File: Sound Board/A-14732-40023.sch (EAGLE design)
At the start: 237 parts, among them P2 AUX IN, P3 AUX OUT, P4 ORKIN R/W, P5 VOLUME, P6 0.156", P7 0.156", Q1 MPS3646, U1 OKI6295, U10 26LS32A, U11 26LS31, U12 27C040-150, U13 27C040-150, U14 YAMAHA 2151, U15 TIL7524, U16 74LS374, U17 74LS174, U18 16L8, U19 74LS11, U2 2064, U20 74LS139, U21 74LS14, U22 74LS74, U23 74LS74, U24 26LS31, U25 26LS32A, U26 74LS04, U28 YAMAHA 3012, U29 LM324D, U3 27C040, U30 MC3340, U31 MB3731, U32 TL084D, U33 TL084D, U4 6809E, U5 74LS374DW, U6 26LS32A, U7 26LS31, U8 74LS138, U9 74LS74, Y1 3.5749MHz, Y2 8MHz

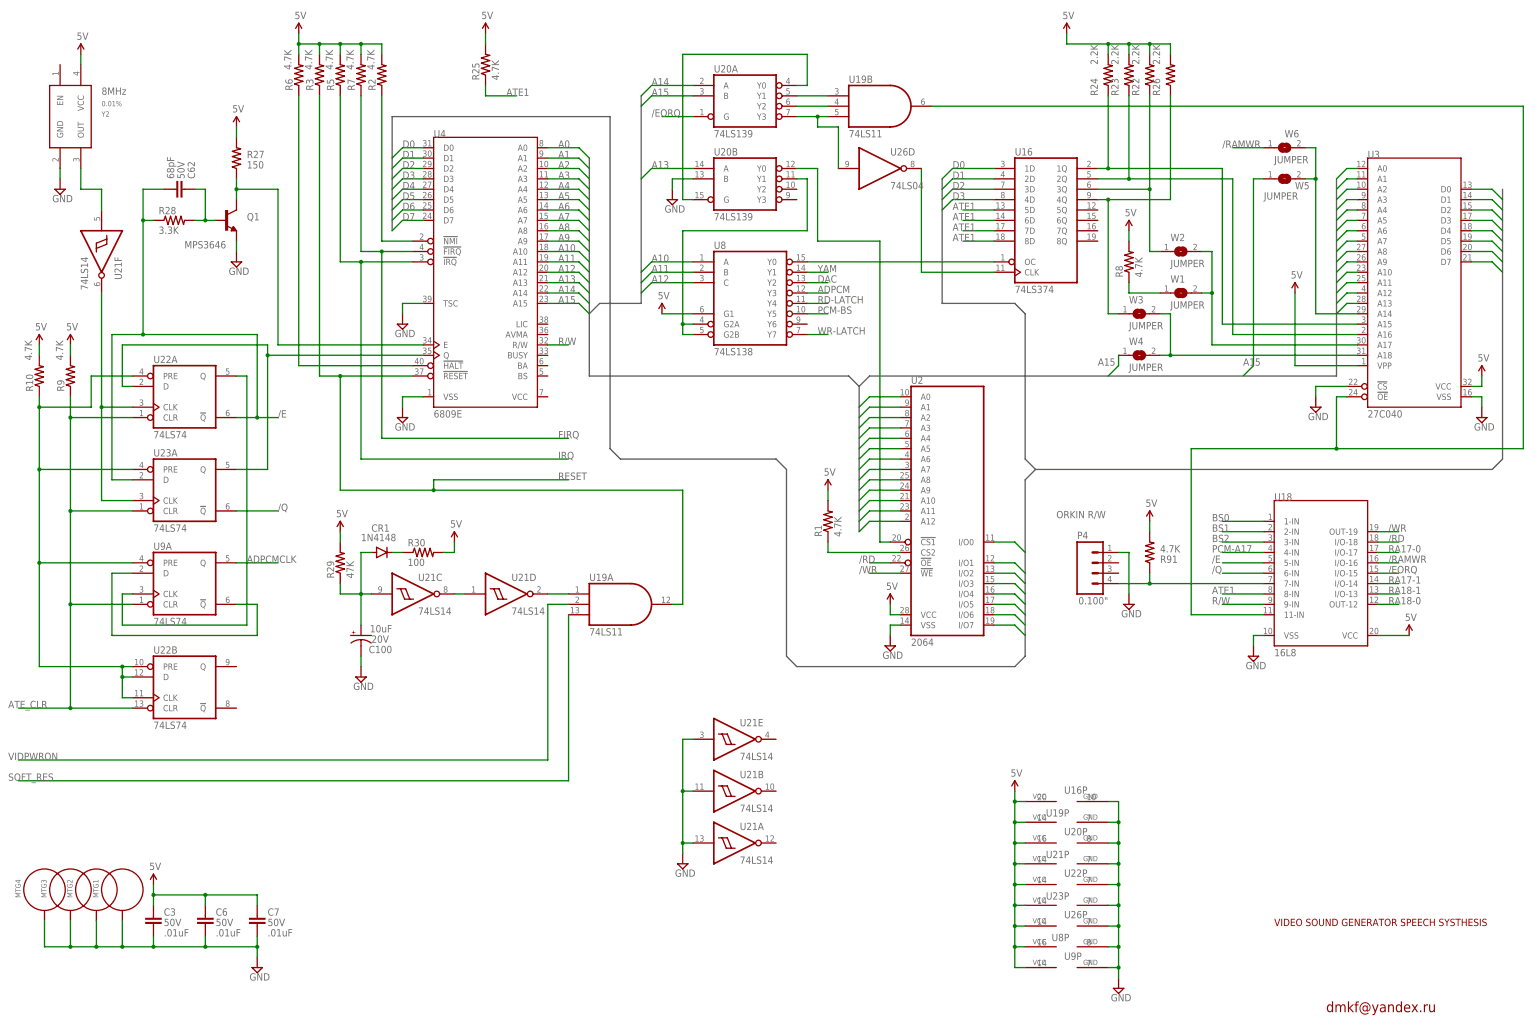
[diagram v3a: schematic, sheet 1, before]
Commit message: replaced all non-power rail resistors to 0805 size 1/8W
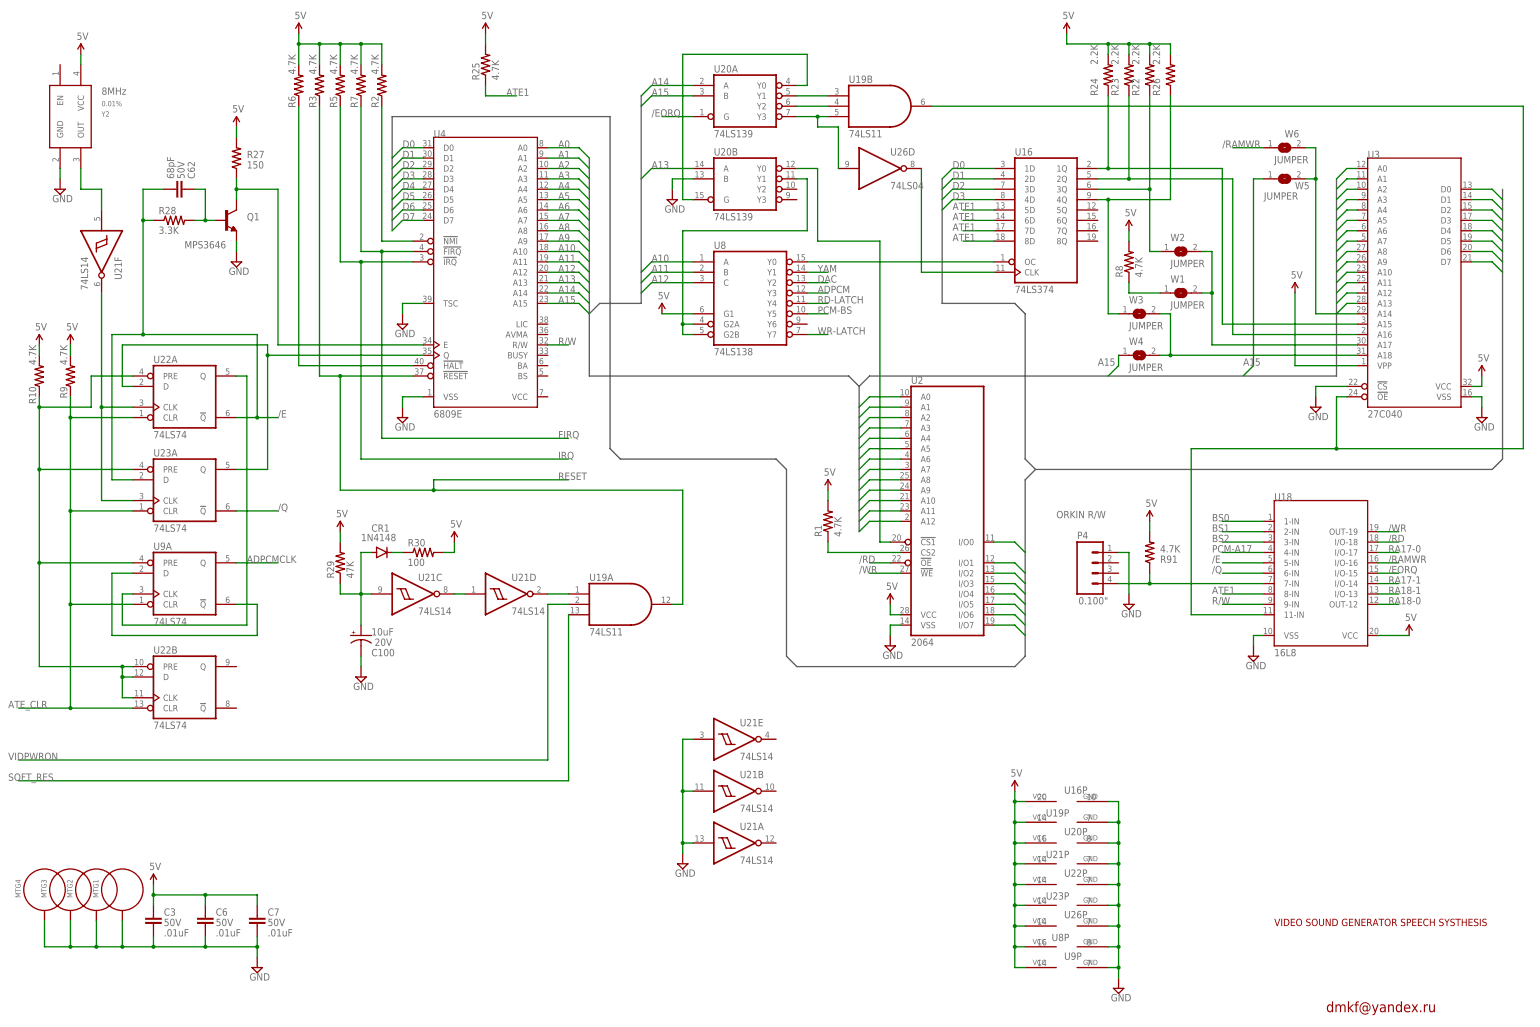
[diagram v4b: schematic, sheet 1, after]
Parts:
- C100: device SparkFun-Capacitors:10UF-16V-10%(TANT) -> A-14732-40023:CAP_POLC
- C3, C6, C61, C62, C7: device SparkFun-Capacitors:1.0UF50V10%(1206) -> SparkFun-Passives:CAP0805
- R10, R11, R12, R13, R14, R19, R2, R20, R21, R22, R23, R24, R25, R26, R28, R29, R3, R32, R33, R34, R35, R36, R37, R38, R39, R4, R40, R41, R42, R43, R44, R45, R46, R48, R5, R51, R52, R53, R55, R59, R6, R60, R61, R62, R63, R64, R67, R68, R69, R7, R71, R77, R78, R79, R80, R81, R84, R85, R86, R87, R88, R9, R91, R92, R93, R94, R95, R96: device resistor:R-US_R1206 -> SparkFun-Passives:RESISTOR0805-RES
- R27, R30, R89: device resistor:R-US_R1206 -> SparkFun-Passives:RESISTOR1206
- U4: device MK-ICs:6809E -> A-14732-40023:6809E
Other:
- moved on the sheet: R2, R3, R5, R6, R7

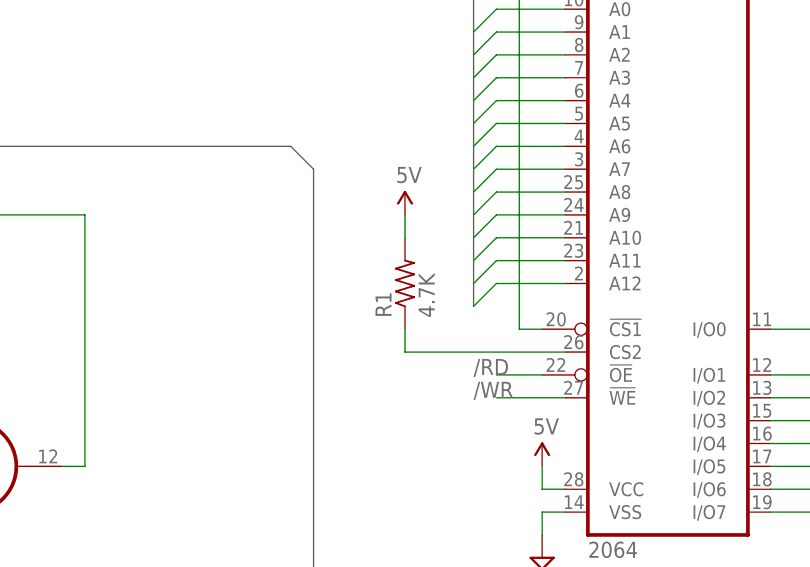
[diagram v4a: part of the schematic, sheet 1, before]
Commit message: replaced filter capacitors to 0805 size
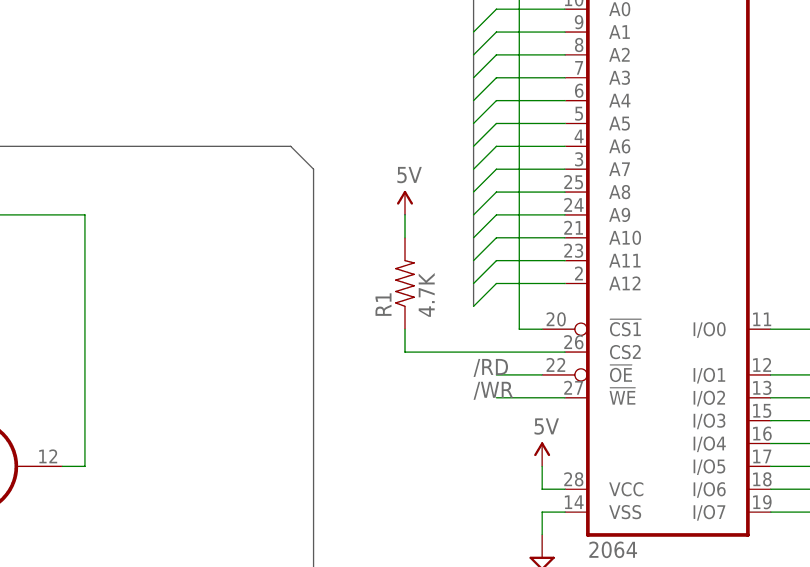
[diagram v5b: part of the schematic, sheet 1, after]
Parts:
- C10, C104, C105, C106, C107, C11, C12, C13, C14, C15, C16, C17, C18, C19, C2, C20, C21, C22, C24, C25, C26, C29, C30, C31, C32, C33, C35, C36, C37, C38, C39, C40, C41, C42, C43, C44, C45, C47, C48, C49, C50, C51, C52, C54, C55, C56, C58, C60, C69, C71, C72, C74, C76, C88, C89, C9, C90, C91, C92, C96, C97, C98, C99: device SparkFun-Capacitors:1.0UF50V10%(1206) -> SparkFun-Passives:CAP0805
- C65: device SparkFun-Capacitors:0.33UF-50V-10%(0805) -> SparkFun-Passives:CAP0805
- R1: device resistor:R-US_R1206 -> SparkFun-Passives:RESISTOR0805-RES

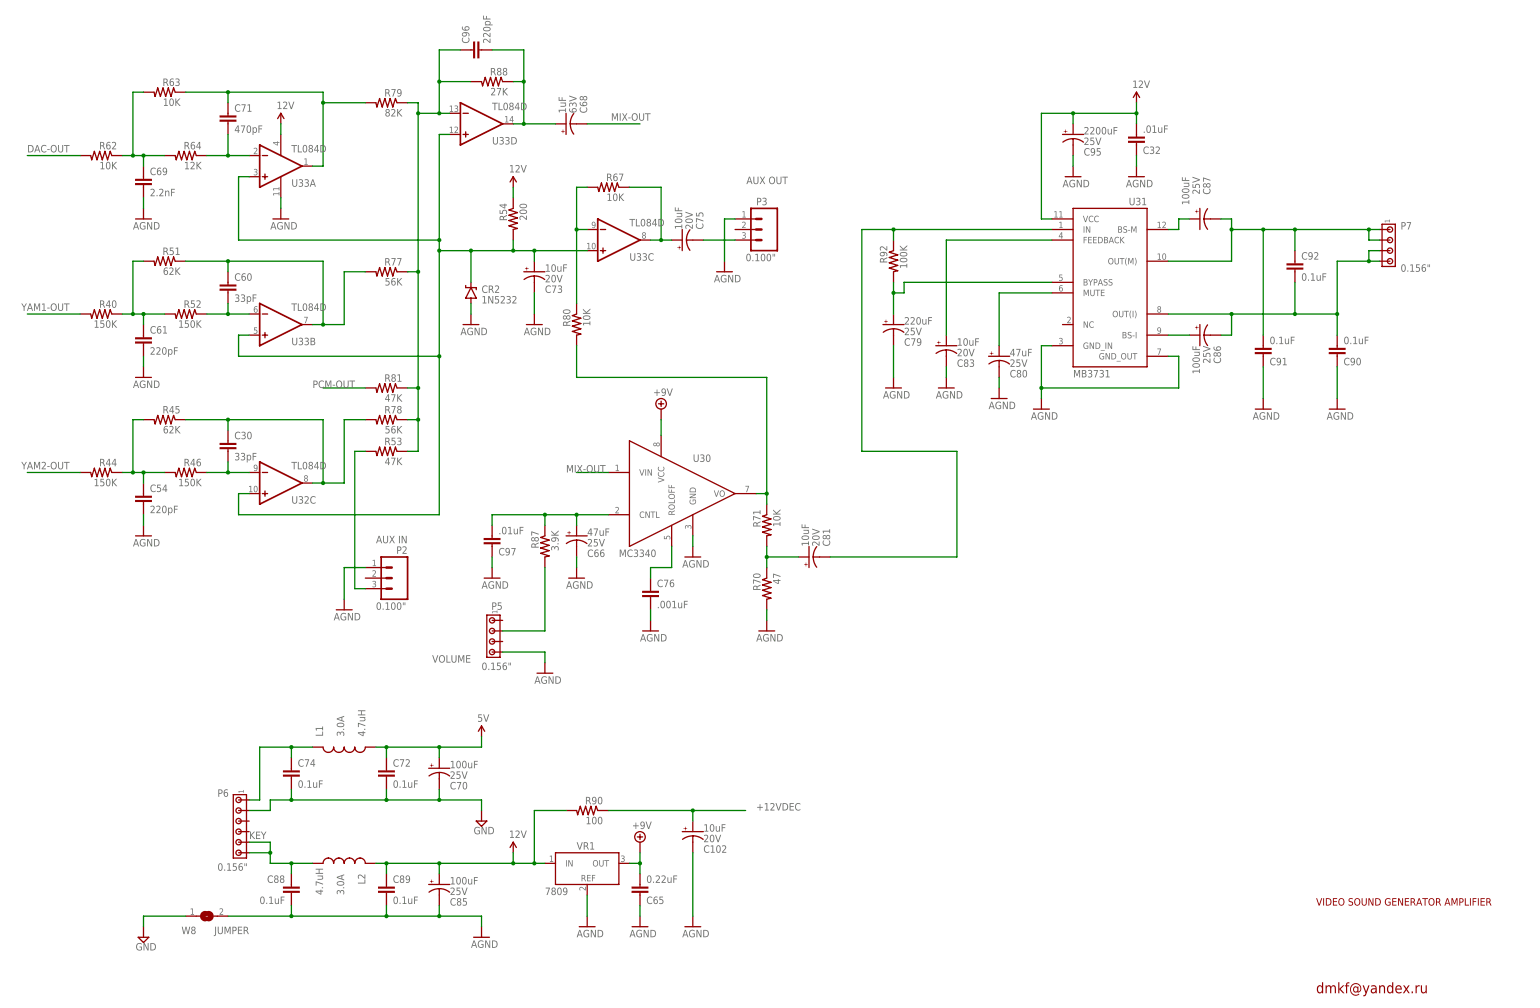
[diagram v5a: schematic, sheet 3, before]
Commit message: replaced all the polarized capacitors with PANASONIC_? package, fixed bugs, replaced C95 with a hole-through
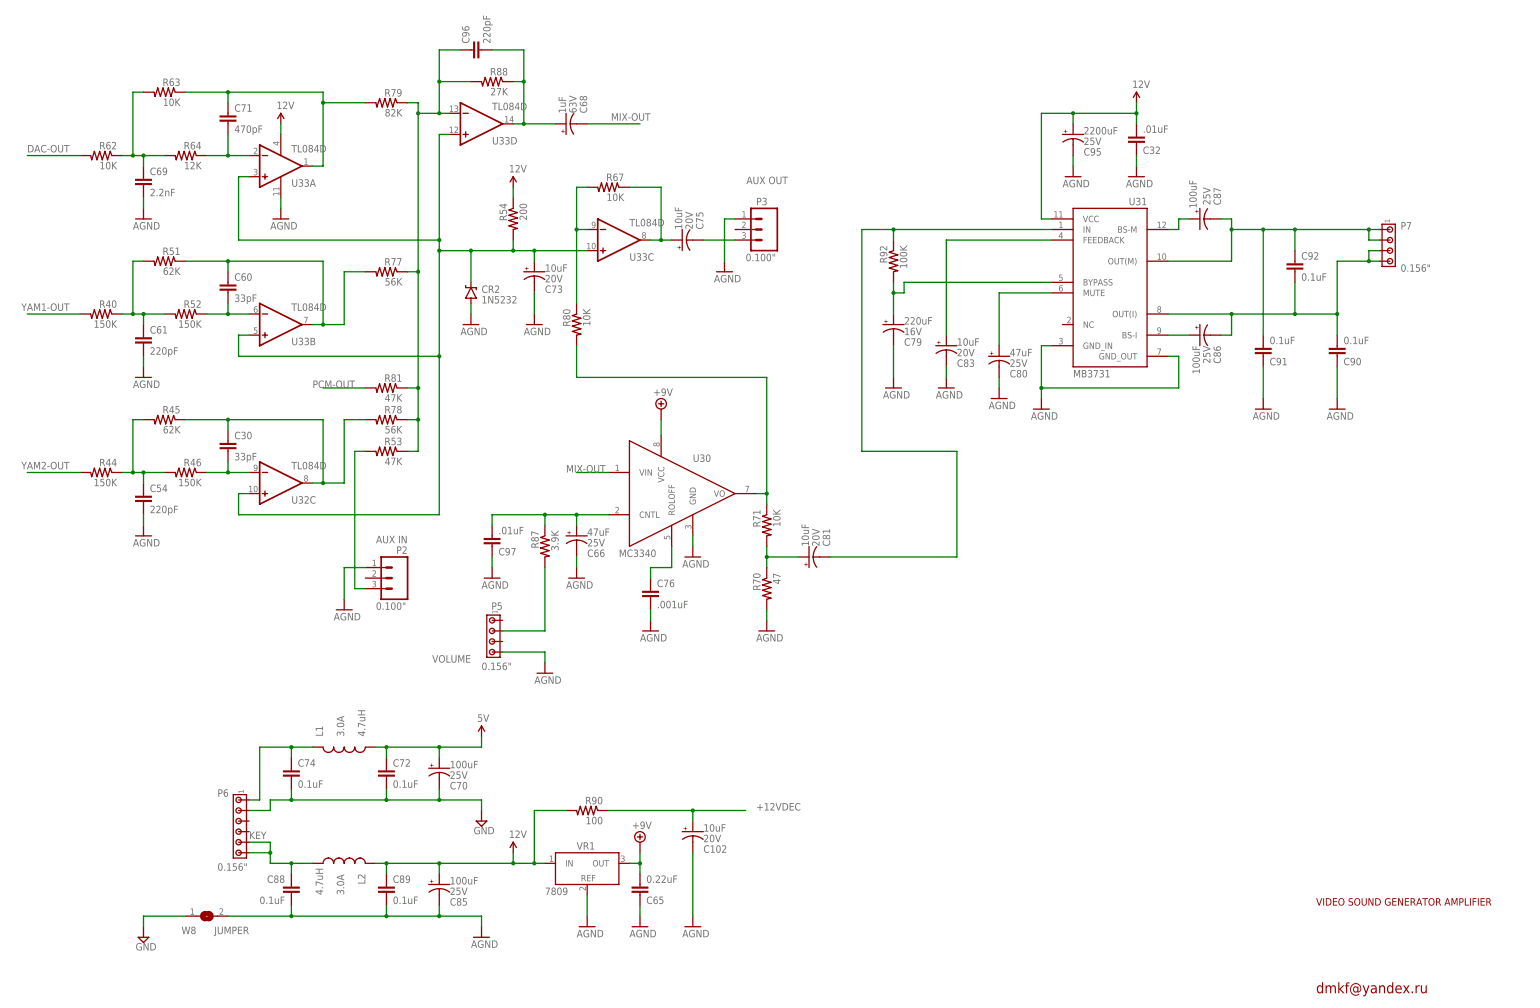
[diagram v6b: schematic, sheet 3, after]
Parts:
- C102, C46, C53, C57, C68, C73, C75, C81, C83: device SparkFun-Capacitors:100UF-63V-20%(ELECT) -> A-14732-40023:CAP_POLC
- C103, C63, C66, C70, C80, C85, C86, C87: device SparkFun-Capacitors:100UF-63V-20%(ELECT) -> A-14732-40023:CAP_POLD
- C64, C67: device SparkFun-Capacitors:100UF-63V-20%(ELECT) -> A-14732-40023:CAP_POLC; VOLTAGE 16V -> 20V
- C79: device SparkFun-Capacitors:100UF-63V-20%(ELECT) -> A-14732-40023:CAP_POLE; VOLTAGE 25V -> 16V
- C95: device SparkFun-Capacitors:100UF-63V-20%(ELECT) -> A-14732-40023:CAP_POLPTH3

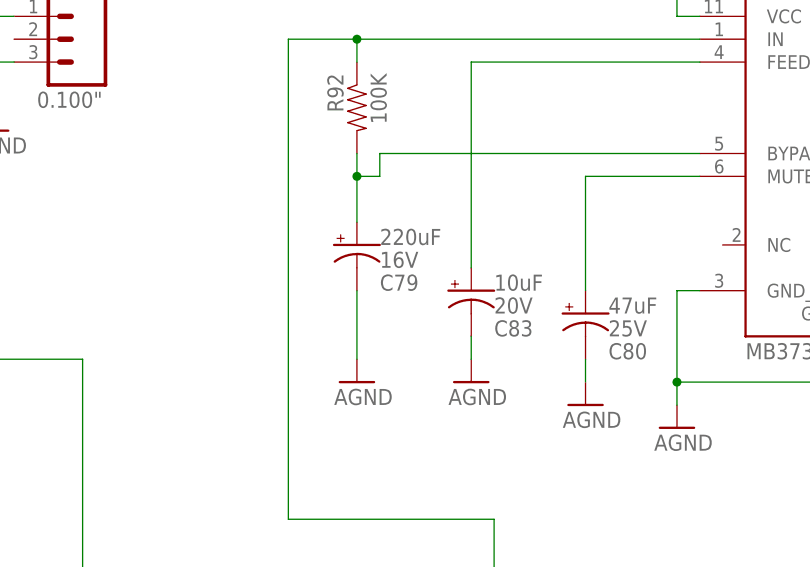
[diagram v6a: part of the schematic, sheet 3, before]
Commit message: C79 corrected to C84
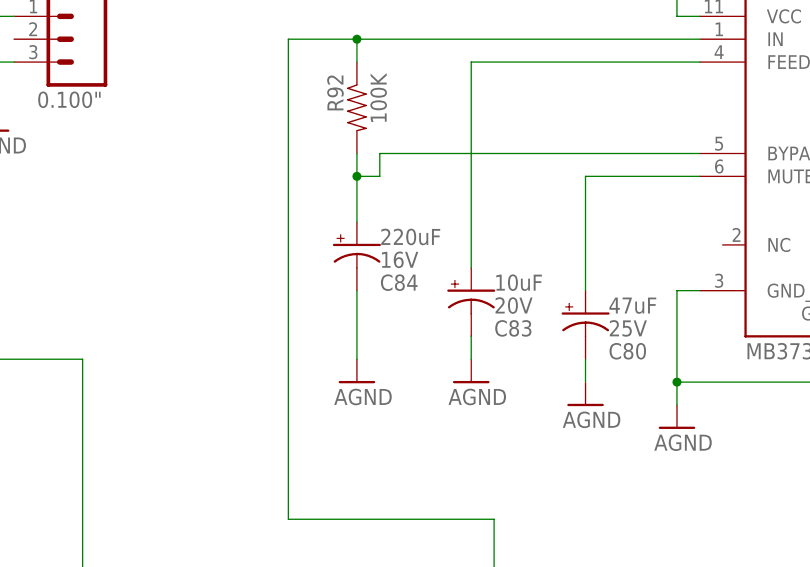
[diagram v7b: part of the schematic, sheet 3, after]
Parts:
- renumbered C79 to C84
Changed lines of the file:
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@@
 <attribute name="TOLERANCE" value="0.01%"/>
 </part>
-<part name="C79" library="A-14732-40023" deviceset="CAP_POL" device="E" value="220uF">
+<part name="C84" library="A-14732-40023" deviceset="CAP_POL" device="E" value="220uF">
 <attribute name="VOLTAGE" value="16V"/>
 </part>
@@
 <attribute name="KEY" x="76.2" y="43.18" size="1.778" layer="96" rot="MR180" display="name"/>
 </instance>
-<instance part="C79" gate="G$1" x="231.14" y="165.1">
+<instance part="C84" gate="G$1" x="231.14" y="165.1">
 <attribute name="VOLTAGE" x="233.68" y="162.56" size="1.778" layer="96"/>
 </instance>
@@
 </segment>
 <segment>
-<pinref part="C79" gate="G$1" pin="-"/>
+<pinref part="C84" gate="G$1" pin="-"/>
 <pinref part="U$37" gate="G$1" pin="AGND"/>
 <wire x1="231.14" y1="160.02" x2="231.14" y2="152.4" width="0.1524" layer="91"/>
@@
 <net name="N$92" class="0">
 <segment>
-<pinref part="C79" gate="G$1" pin="+"/>
+<pinref part="C84" gate="G$1" pin="+"/>
 <wire x1="269.24" y1="175.26" x2="233.68" y2="175.26" width="0.1524" layer="91"/>
 <wire x1="233.68" y1="175.26" x2="233.68" y2="172.72" width="0.1524" layer="91"/>

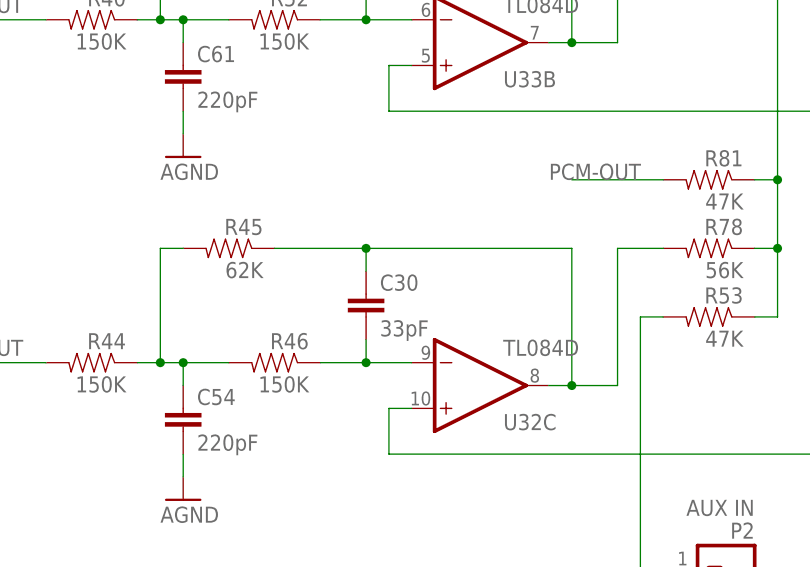
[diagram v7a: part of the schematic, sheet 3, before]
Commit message: corrected C30 to C59
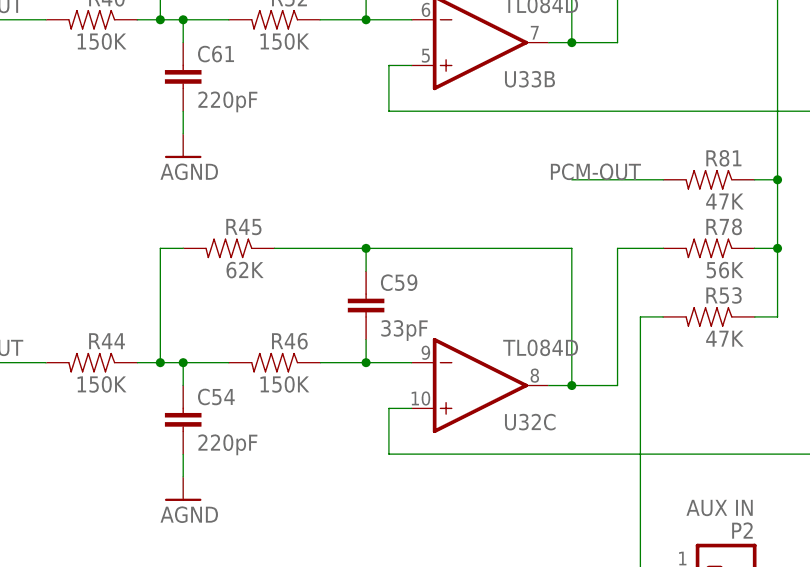
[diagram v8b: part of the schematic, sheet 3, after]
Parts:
- renumbered C30 to C59
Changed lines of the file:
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@@
 <part name="U$21" library="SparkFun-Aesthetics" deviceset="AGND" device=""/>
 <part name="R45" library="SparkFun-Passives" deviceset="RESISTOR" device="0805-RES" value="62K"/>
-<part name="C30" library="SparkFun-Passives" deviceset="CAP" device="0805" value="33pF">
+<part name="C59" library="SparkFun-Passives" deviceset="CAP" device="0805" value="33pF">
 <attribute name="VOLTAGE" value="50V"/>
 </part>
@@
 <instance part="U$21" gate="G$1" x="50.8" y="114.3"/>
 <instance part="R45" gate="G$1" x="55.88" y="142.24" rot="MR0"/>
-<instance part="C30" gate="G$1" x="71.12" y="134.62"/>
+<instance part="C59" gate="G$1" x="71.12" y="134.62"/>
 <instance part="R78" gate="G$1" x="109.22" y="142.24" rot="MR0"/>
 <instance part="R81" gate="G$1" x="109.22" y="149.86" rot="MR0"/>
@@
 <segment>
 <pinref part="R45" gate="G$1" pin="1"/>
-<pinref part="C30" gate="G$1" pin="1"/>
+<pinref part="C59" gate="G$1" pin="1"/>
 <wire x1="60.96" y1="142.24" x2="71.12" y2="142.24" width="0.1524" layer="91"/>
 <wire x1="71.12" y1="142.24" x2="71.12" y2="139.7" width="0.1524" layer="91"/>
@@
 <segment>
 <pinref part="R46" gate="G$1" pin="1"/>
-<pinref part="C30" gate="G$1" pin="2"/>
+<pinref part="C59" gate="G$1" pin="2"/>
 <wire x1="71.12" y1="129.54" x2="76.2" y2="129.54" width="0.1524" layer="91"/>
 <wire x1="71.12" y1="132.08" x2="71.12" y2="129.54" width="0.1524" layer="91"/>
